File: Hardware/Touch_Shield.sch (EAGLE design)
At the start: 17 parts, among them IC1 MPR121, Q1 BSS138, Q2 BSS138, U1 ARDUINO_SHIELDLABEL

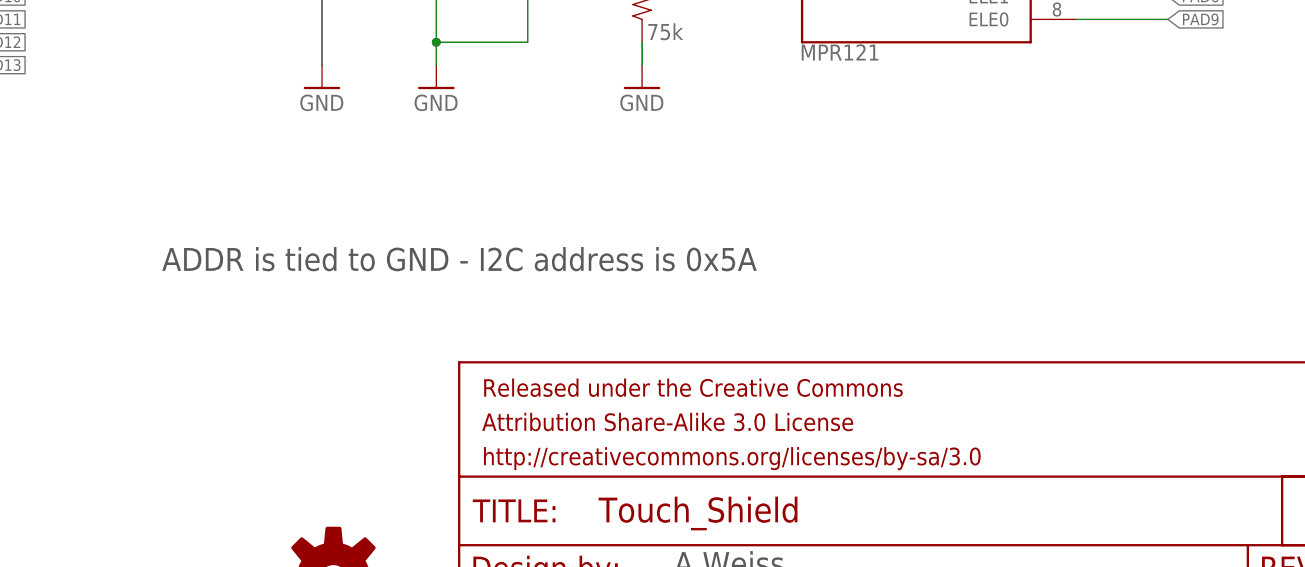
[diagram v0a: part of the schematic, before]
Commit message: Adding schematic note about selectable I2C address
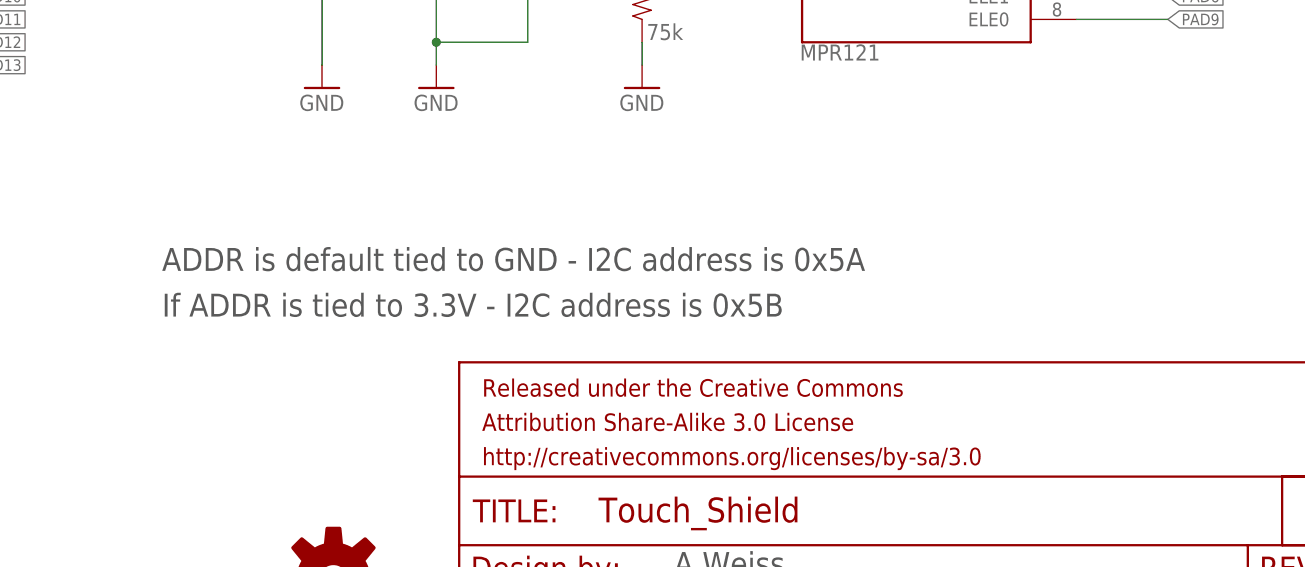
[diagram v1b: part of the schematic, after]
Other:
- note added: "ADDR is default tied to GND - I2C address is 0x5A"
- note added: "If ADDR is tied to 3.3V - I2C address is 0x5B"
- note removed: "ADDR is tied to GND - I2C address is 0x5A"
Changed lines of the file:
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@@
 <plain>
 <text x="171.196" y="11.938" size="2.54" layer="97">A.Weiss</text>
-<text x="114.3" y="45.72" size="2.54" layer="97">ADDR is tied to GND - I2C address is 0x5A</text>
+<text x="114.3" y="45.72" size="2.54" layer="97">ADDR is default tied to GND - I2C address is 0x5A</text>
 <text x="238.76" y="7.62" size="2.54" layer="97" font="vector">v12</text>
 <text x="176.276" y="6.858" size="2.54" layer="97">T. Klopfenstein</text>
+<text x="114.3" y="40.64" size="2.54" layer="97">If ADDR is tied to 3.3V - I2C address is 0x5B</text>
 </plain>
 <instances>

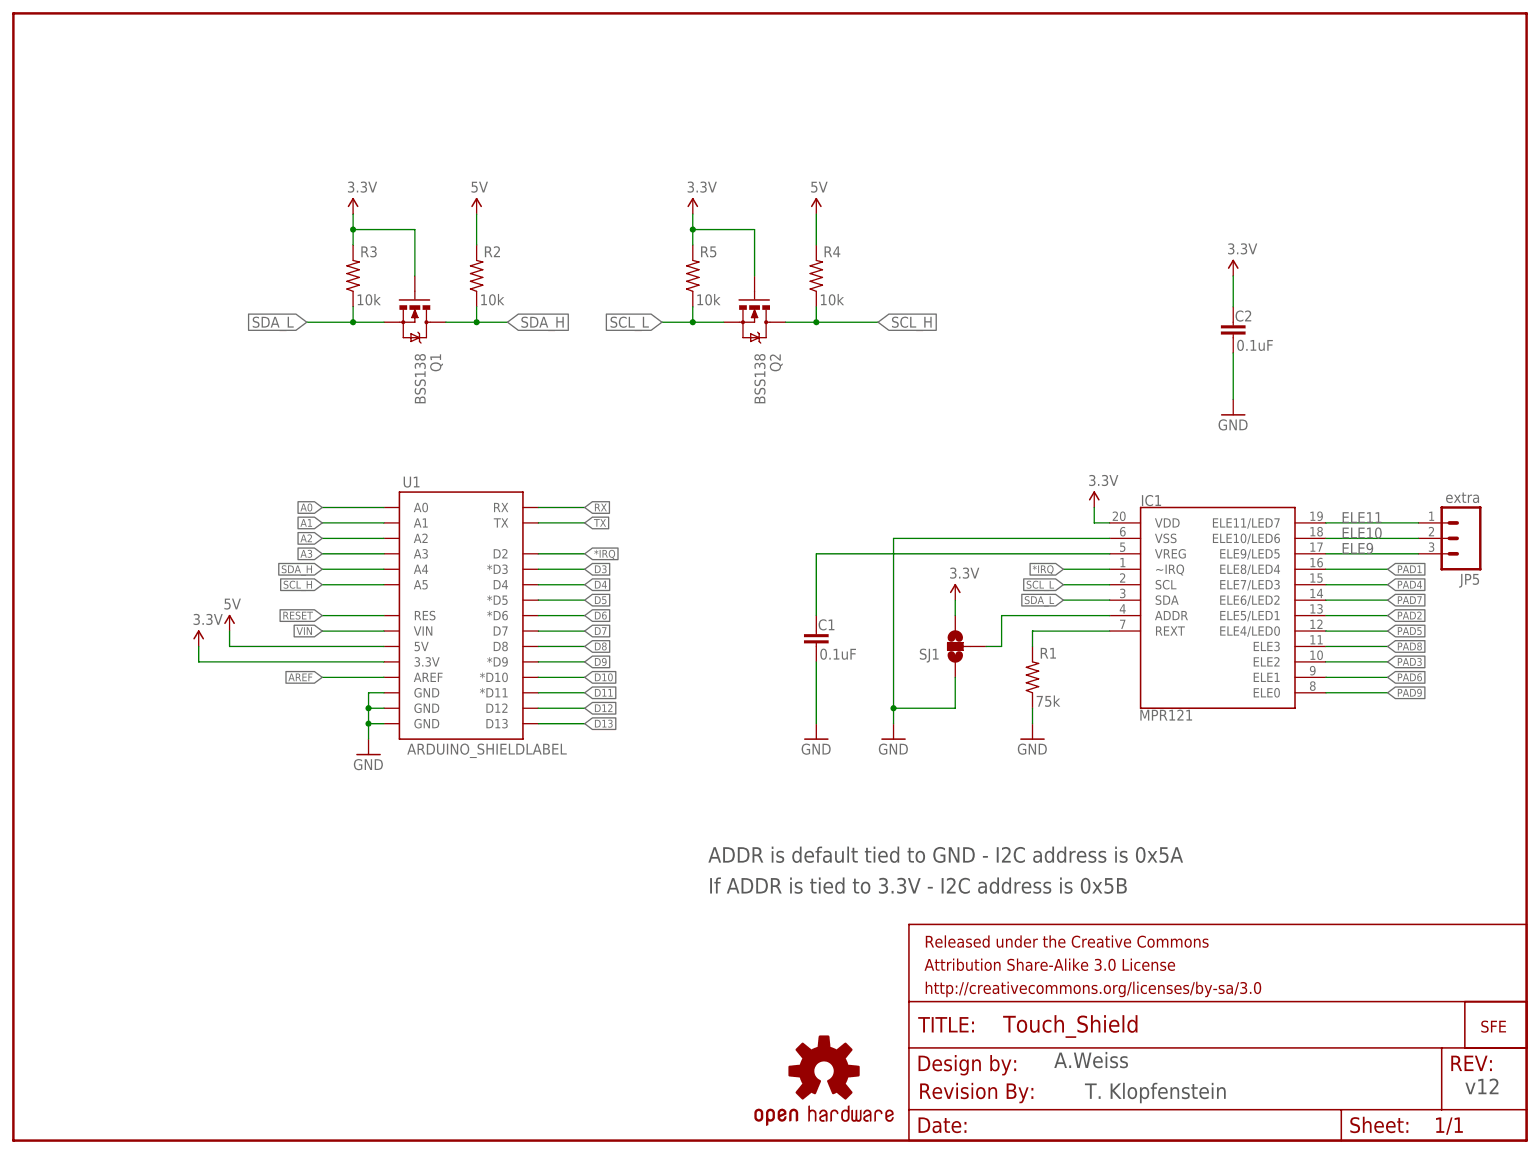
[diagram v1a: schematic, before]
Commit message: Updating shield layout to R3
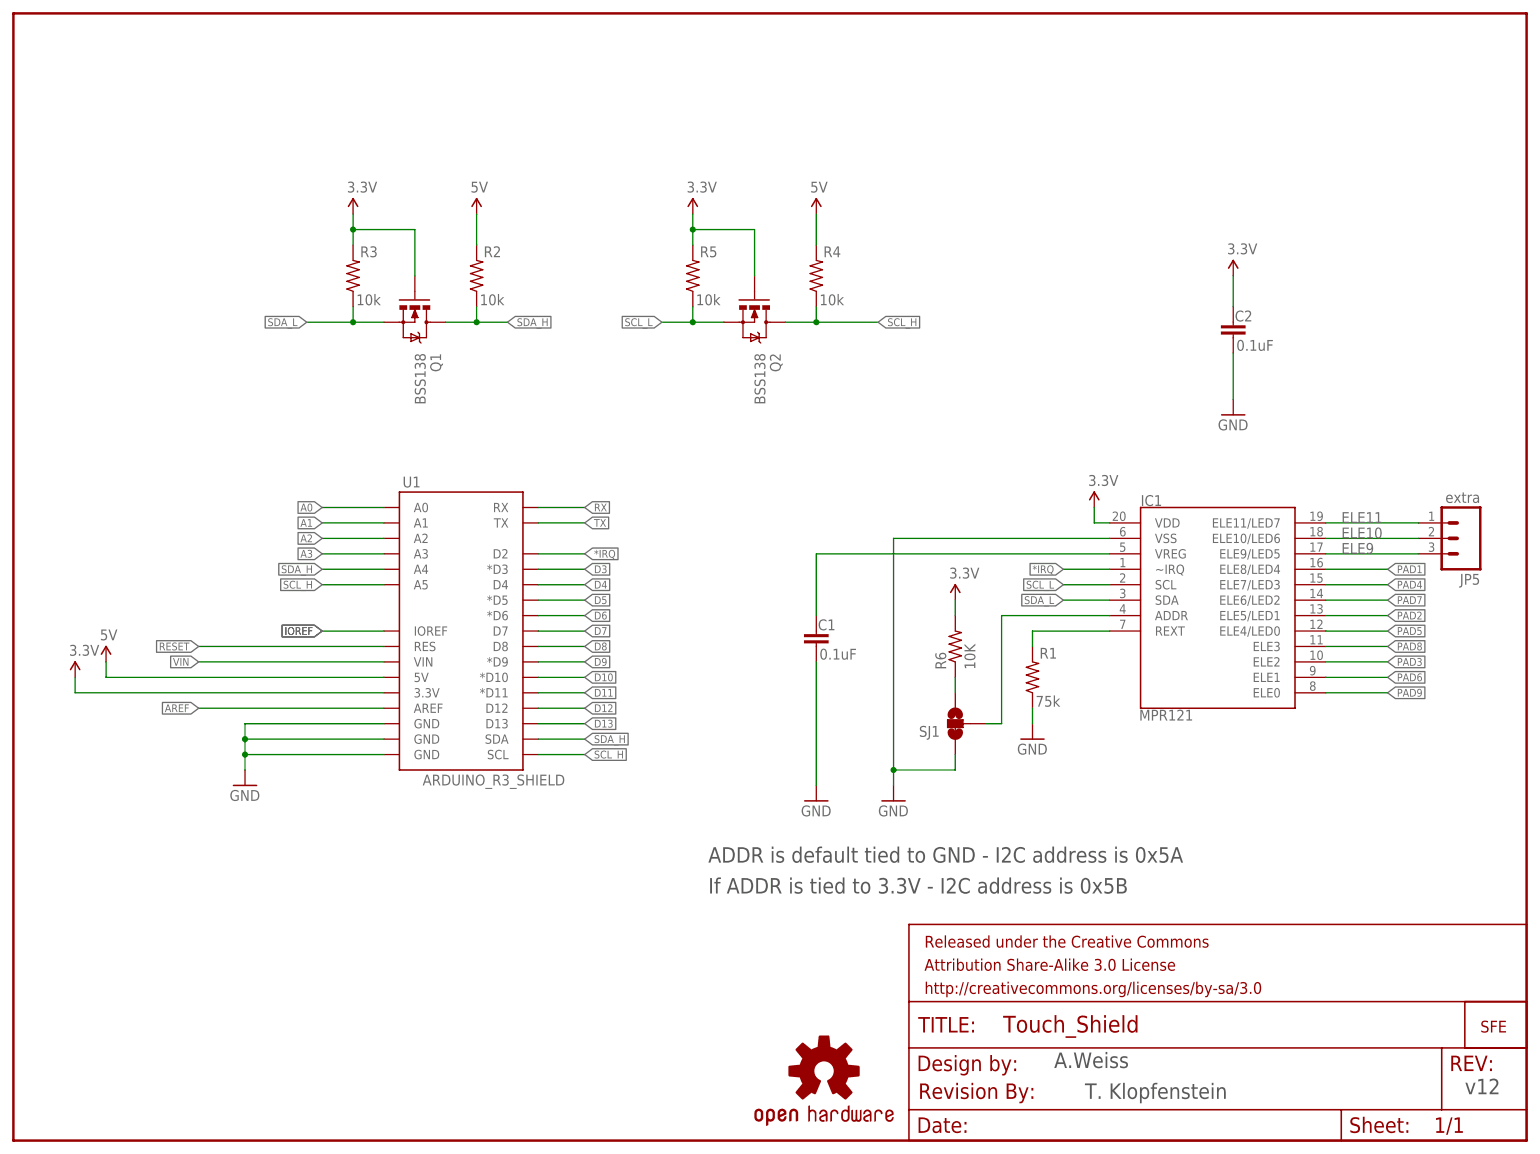
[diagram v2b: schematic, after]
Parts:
- added R6: 10K, SparkFun-Resistors:10KOHM1/10W1%(0603)0603
- U1: value ARDUINO_SHIELDLABEL -> ARDUINO_R3_SHIELD; device SparkFun:ARDUINO_SHIELDLABEL -> SparkFun-Boards:ARDUINO_R3_SHIELD
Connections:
- new net IOREF: U1.IOREF
- new net N$2: R6.1, SJ1.3
- net 3.3V: now also R6.2; no longer SJ1.3
- net SCL_H: now also U1.SCL
- net SDA_H: now also U1.SDA
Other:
- moved on the sheet: SJ1

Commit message: Updating all the resistors to the same production ID number
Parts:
- R2, R3, R4, R5: device SparkFun:RESISTOR0603-RES -> SparkFun-Resistors:10KOHM1/10W1%(0603)0603
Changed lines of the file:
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@@
 <part name="GND6" library="SparkFun" deviceset="GND" device=""/>
 <part name="JP5" library="SparkFun" deviceset="M03" device="PTH" value="extra"/>
-<part name="R2" library="SparkFun" deviceset="RESISTOR" device="0603-RES" value="10k"/>
+<part name="R2" library="SparkFun-Resistors" deviceset="10KOHM1/10W1%(0603)" device="0603" value="10k"/>
 <part name="P+1" library="SparkFun" deviceset="3.3V" device=""/>
 <part name="P+2" library="SparkFun" deviceset="3.3V" device=""/>
@@
 <part name="P+4" library="SparkFun" deviceset="3.3V" device=""/>
 <part name="Q1" library="SparkFun" deviceset="MOSFET-NCHANNEL" device="SMD" value="BSS138"/>
-<part name="R4" library="SparkFun" deviceset="RESISTOR" device="0603-RES" value="10k"/>
+<part name="R4" library="SparkFun-Resistors" deviceset="10KOHM1/10W1%(0603)" device="0603" value="10k"/>
 <part name="U$2" library="SparkFun" deviceset="5V" device=""/>
 <part name="P+5" library="SparkFun" deviceset="3.3V" device=""/>
 <part name="Q2" library="SparkFun" deviceset="MOSFET-NCHANNEL" device="SMD" value="BSS138"/>
-<part name="R3" library="SparkFun" deviceset="RESISTOR" device="0603-RES" value="10k"/>
-<part name="R5" library="SparkFun" deviceset="RESISTOR" device="0603-RES" value="10k"/>
+<part name="R3" library="SparkFun-Resistors" deviceset="10KOHM1/10W1%(0603)" device="0603" value="10k"/>
+<part name="R5" library="SparkFun-Resistors" deviceset="10KOHM1/10W1%(0603)" device="0603" value="10k"/>
 <part name="U$5" library="SparkFun-Aesthetics" deviceset="OSHW-LOGO" device="L"/>
 <part name="U$1" library="SparkFun-Aesthetics" deviceset="REVISION" device=""/>

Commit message: Re-panelized and added fiducials to board
I re-did the panel to 4 boards and added local fiducials
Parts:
- added FID1, FID2: FIDUCIALUFIDUCIAL, SparkFun-Aesthetics:FIDUCIALUFIDUCIAL
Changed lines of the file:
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@@
 <?xml version="1.0" encoding="utf-8"?>
 <!DOCTYPE eagle SYSTEM "eagle.dtd">
-<eagle version="6.4">
+<eagle version="6.5.0">
 <drawing>
 <settings>
@@
 <grid distance="0.1" unitdist="inch" unit="inch" style="lines" multiple="1" display="no" altdistance="0.01" altunitdist="inch" altunit="inch"/>
 <layers>
-<layer number="1" name="Top" color="4" fill="1" visible="yes" active="no"/>
-<layer number="2" name="Route2" color="1" fill="3" visible="yes" active="no"/>
-<layer number="3" name="Route3" color="4" fill="3" visible="yes" active="no"/>
-<layer number="4" name="Route4" color="1" fill="4" visible="yes" active="no"/>
-<layer number="5" name="Route5" color="4" fill="4" visible="yes" active="no"/>
-<layer number="6" name="Route6" color="1" fill="8" visible="yes" active="no"/>
-<layer number="7" name="Route7" color="4" fill="8" visible="yes" active="no"/>
-<layer number="8" name="Route8" color="1" fill="2" visible="yes" active="no"/>
-<layer number="9" name="Route9" color="4" fill="2" visible="yes" active="no"/>
-<layer number="10" name="Route10" color="1" fill="7" visible="yes" active="no"/>
-<layer number="11" name="Route11" color="4" fill="7" visible="yes" active="no"/>
-<layer number="12" name="Route12" color="1" fill="5" visible="yes" active="no"/>
-<layer number="13" name="Route13" color="4" fill="5" visible="yes" active="no"/>
-<layer number="14" name="Route14" color="1" fill="6" visible="yes" active="no"/>
-<layer number="15" name="Route15" color="4" fill="6" visible="yes" active="no"/>
-<layer number="16" name="Bottom" color="1" fill="1" visible="yes" active="no"/>
-<layer number="17" name="Pads" color="2" fill="1" visible="yes" active="no"/>
-<layer number="18" name="Vias" color="2" fill="1" visible="yes" active="no"/>
-<layer number="19" name="Unrouted" color="6" fill="1" visible="yes" active="no"/>
-<layer number="20" name="Dimension" color="15" fill="1" visible="yes" active="no"/>
-<layer number="21" name="tPlace" color="16" fill="1" visible="yes" active="no"/>
-<layer number="22" name="bPlace" color="14" fill="1" visible="yes" active="no"/>
-<layer number="23" name="tOrigins" color="15" fill="1" visible="yes" active="no"/>
-<layer number="24" name="bOrigins" color="15" fill="1" visible="yes" active="no"/>
-<layer number="25" name="tNames" color="7" fill="1" visible="yes" active="no"/>
-<layer number="26" name="bNames" color="7" fill="1" visible="yes" active="no"/>
-<layer number="27" name="tValues" color="7" fill="1" visible="yes" active="no"/>
-<layer number="28" name="bValues" color="7" fill="1" visible="yes" active="no"/>
+<layer number="1" name="Top" color="4" fill="1" visible="no" active="no"/>
+<layer number="2" name="Route2" color="1" fill="3" visible="no" active="no"/>
+<layer number="3" name="Route3" color="4" fill="3" visible="no" active="no"/>
+<layer number="4" name="Route4" color="1" fill="4" visible="no" active="no"/>
+<layer number="5" name="Route5" color="4" fill="4" visible="no" active="no"/>
+<layer number="6" name="Route6" color="1" fill="8" visible="no" active="no"/>
+<layer number="7" name="Route7" color="4" fill="8" visible="no" active="no"/>
+<layer number="8" name="Route8" color="1" fill="2" visible="no" active="no"/>
+<layer number="9" name="Route9" color="4" fill="2" visible="no" active="no"/>
+<layer number="10" name="Route10" color="1" fill="7" visible="no" active="no"/>
+<layer number="11" name="Route11" color="4" fill="7" visible="no" active="no"/>
+<layer number="12" name="Route12" color="1" fill="5" visible="no" active="no"/>
+<layer number="13" name="Route13" color="4" fill="5" visible="no" active="no"/>
+<layer number="14" name="Route14" color="1" fill="6" visible="no" active="no"/>
+<layer number="15" name="Route15" color="4" fill="6" visible="no" active="no"/>
+<layer number="16" name="Bottom" color="1" fill="1" visible="no" active="no"/>
+<layer number="17" name="Pads" color="2" fill="1" visible="no" active="no"/>
+<layer number="18" name="Vias" color="2" fill="1" visible="no" active="no"/>
+<layer number="19" name="Unrouted" color="6" fill="1" visible="no" active="no"/>
+<layer number="20" name="Dimension" color="15" fill="1" visible="no" active="no"/>
+<layer number="21" name="tPlace" color="16" fill="1" visible="no" active="no"/>
+<layer number="22" name="bPlace" color="14" fill="1" visible="no" active="no"/>
+<layer number="23" name="tOrigins" color="15" fill="1" visible="no" active="no"/>
+<layer number="24" name="bOrigins" color="15" fill="1" visible="no" active="no"/>
+<layer number="25" name="tNames" color="7" fill="1" visible="no" active="no"/>
+<layer number="26" name="bNames" color="7" fill="1" visible="no" active="no"/>
+<layer number="27" name="tValues" color="7" fill="1" visible="no" active="no"/>
+<layer number="28" name="bValues" color="7" fill="1" visible="no" active="no"/>
 <layer number="29" name="tStop" color="7" fill="3" visible="no" active="no"/>
 <layer number="30" name="bStop" color="7" fill="6" visible="no" active="no"/>
@@
 <layer number="35" name="tGlue" color="7" fill="4" visible="no" active="no"/>
 <layer number="36" name="bGlue" color="7" fill="5" visible="no" active="no"/>
-<layer number="37" name="tTest" color="7" fill="1" visible="yes" active="no"/>
-<layer number="38" name="bTest" color="7" fill="1" visible="yes" active="no"/>
+<layer number="37" name="tTest" color="7" fill="1" visible="no" active="no"/>
+<layer number="38" name="bTest" color="7" fill="1" visible="no" active="no"/>
 <layer number="39" name="tKeepout" color="4" fill="11" visible="no" active="no"/>
 <layer number="40" name="bKeepout" color="1" fill="11" visible="no" active="no"/>
@@
 <layer number="44" name="Drills" color="7" fill="1" visible="no" active="no"/>
 <layer number="45" name="Holes" color="7" fill="1" visible="no" active="no"/>
-<layer number="46" name="Milling" color="3" fill="1" visible="yes" active="no"/>
-<layer number="47" name="Measures" color="7" fill="1" visible="yes" active="no"/>
-<layer number="48" name="Document" color="7" fill="1" visible="yes" active="no"/>
-<layer number="49" name="Reference" color="13" fill="1" visible="yes" active="no"/>
-<layer number="50" name="dxf" color="7" fill="1" visible="yes" active="no"/>
-<layer number="51" name="tDocu" color="6" fill="1" visible="yes" active="no"/>
-<layer number="52" name="bDocu" color="7" fill="1" visible="yes" active="no"/>
-<layer number="53" name="tGND_GNDA" color="7" fill="9" visible="yes" active="no"/>
-<layer number="54" name="bGND_GNDA" color="1" fill="9" visible="yes" active="no"/>
-<layer number="56" name="wert" color="7" fill="1" visible="yes" active="no"/>
+<layer number="46" name="Milling" color="3" fill="1" visible="no" active="no"/>
+<layer number="47" name="Measures" color="7" fill="1" visible="no" active="no"/>
+<layer number="48" name="Document" color="7" fill="1" visible="no" active="no"/>
+<layer number="49" name="Reference" color="13" fill="1" visible="no" active="no"/>
+<layer number="50" name="dxf" color="7" fill="1" visible="no" active="no"/>
+<layer number="51" name="tDocu" color="6" fill="1" visible="no" active="no"/>
+<layer number="52" name="bDocu" color="7" fill="1" visible="no" active="no"/>
+<layer number="53" name="tGND_GNDA" color="7" fill="9" visible="no" active="no"/>
+<layer number="54" name="bGND_GNDA" color="1" fill="9" visible="no" active="no"/>
+<layer number="56" name="wert" color="7" fill="1" visible="no" active="no"/>
 <layer number="91" name="Nets" color="2" fill="1" visible="yes" active="yes"/>
 <layer number="92" name="Busses" color="1" fill="1" visible="yes" active="yes"/>
@@
 <part name="P+6" library="SparkFun" deviceset="3.3V" device=""/>
 <part name="R6" library="SparkFun-Resistors" deviceset="10KOHM1/10W1%(0603)" device="0603" value="10K"/>
+<part name="FID1" library="SparkFun-Aesthetics" deviceset="FIDUCIAL" device="UFIDUCIAL"/>
+<part name="FID2" library="SparkFun-Aesthetics" deviceset="FIDUCIAL" device="UFIDUCIAL"/>
 </parts>
 <sheets>
@@
 <instance part="P+6" gate="G$1" x="154.94" y="88.9"/>
 <instance part="R6" gate="G$1" x="154.94" y="81.28" rot="R90"/>
+<instance part="FID1" gate="G$1" x="223.52" y="38.1"/>
+<instance part="FID2" gate="G$1" x="228.6" y="38.1"/>
 </instances>
 <busses>
